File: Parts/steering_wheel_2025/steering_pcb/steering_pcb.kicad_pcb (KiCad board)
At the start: 2 copper layers, 102 x 102 mm, 189 parts, among them J0 Quick_connector, J1 Button 1 molex-µfit connector, J10 Button 1 molex-µfit connector, J11 Button 1 molex-µfit connector, J12 Button 1 molex-µfit connector, J13 PINHD_1x1_Male, J15 CAN pin header, J2 Button 1 molex-µfit connector, J3 Button 1 molex-µfit connector, J4 Button 1 molex-µfit connector, J5 Button 1 molex-µfit connector, J6 Button 1 molex-µfit connector, J7 Button 1 molex-µfit connector, J8 Button 1 molex-µfit connector, J9 Button 1 molex-µfit connector, Q1 BSS138BKS, Q10 2N7002DW, Q11 2N7002DW, Q12 2N7002DW, Q13 2N7002DW, Q14 2N7002DW, Q15 2N7002DW, Q16 2N7002DW, Q17 2N7002DW, Q18 2N7002DW, Q19 2N7002DW, Q2 2N7002DW, Q20 2N7002DW, Q21 2N7002DW, Q3 2N7002DW, Q4 BS170, Q5 2N7002DW, Q6 BSS138BKS, Q7 2N7002DW, Q8 2N7002DW, Q9 2N7002DW, SW1 Push_Button, U1 MCP2515-xSO, U2 TPS5430DDA, U3 TPS5430DDA, U5 ISM330DHCX, U6 TJA1051T-3, Y1 16MHz

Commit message: pcb progress backup
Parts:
- moved R84 434.1 mm to (132.4, 73.8), turned to 180 degrees
- moved J12 432.8 mm to (139.4, 82.7)
- moved R82 430.7 mm to (141.7, 75.1), turned to 0 degrees
- moved DZ12 427.7 mm to (138.3, 87.2), turned to 180 degrees
- moved R78 422.4 mm to (132.4, 68.5), turned to 0 degrees
- moved R81 419.3 mm to (144.8, 81.1), turned to 0 degrees
- moved D12 419.0 mm to (143.8, 87.2), turned to 0 degrees
- moved R76 416.9 mm to (151.9, 69.2), turned to 90 degrees
- moved J11 416.5 mm to (147.0, 68.0)
- moved Q21 415.3 mm to (145.1, 83.5), turned to 0 degrees
- moved Q19 413.6 mm to (150.0, 74.8)
- moved D11 413.4 mm to (146.8, 76.4)
- moved DZ11 413.3 mm to (146.8, 72.8)
- moved R75 412.6 mm to (149.4, 71.9), turned to 180 degrees
- moved R79 412.3 mm to (145.3, 79.2)
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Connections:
- net /LED and Buttons/Connector_5/button_2_0 renamed button10_0
- net /LED and Buttons/Connector_5/button_2_1 renamed button10_1
- net /LED and Buttons/Connector_5/button_2_2 renamed button10_2
- net /LED and Buttons/Connector_5/button_2_3 renamed button10_3
- net /LED and Buttons/Connector_6/button_1_0 renamed button11_0
- net /LED and Buttons/Connector_6/button_1_1 renamed button11_1
- net /LED and Buttons/Connector_6/button_1_2 renamed button11_2
- net /LED and Buttons/Connector_6/button_1_3 renamed button11_3
- net /LED and Buttons/Connector_6/button_2_0 renamed button12_0
- net /LED and Buttons/Connector_6/button_2_1 renamed button12_1
- net /LED and Buttons/Connector_6/button_2_2 renamed button12_2
- net /LED and Buttons/Connector_6/button_2_3 renamed button12_3
- A1 pad D10: unconnected-(A1-PadD10) -> button7_3
- A1 pad D11: unconnected-(A1-PadD11) -> button7_1
- A1 pad D12: unconnected-(A1-PadD12) -> button7_2
- A1 pad D13: unconnected-(A1-PadD13) -> button7_0
- A1 pad D14: unconnected-(A1-D14/TX3-PadD14) -> button9_3
- A1 pad D3: unconnected-(A1-D3_INT1-PadD3) -> button9_1
- A1 pad D4: unconnected-(A1-PadD4) -> button9_2
- A1 pad D5: unconnected-(A1-PadD5) -> button9_0
- A1 pad D6: unconnected-(A1-PadD6) -> button8_3
- A1 pad D7: unconnected-(A1-PadD7) -> button8_2
- A1 pad D8: unconnected-(A1-PadD8) -> button8_1
- A1 pad D9: unconnected-(A1-PadD9) -> button8_0
- D7 pad 4: /LED and Buttons/Connector_4/button_1_3 -> button7_3
- D7 pad 5: /LED and Buttons/Connector_4/button_1_2 -> button7_2
- D7 pad 6: /LED and Buttons/Connector_4/button_1_1 -> button7_1
- D8 pad 4: /LED and Buttons/Connector_4/button_2_3 -> button8_3
- D8 pad 5: /LED and Buttons/Connector_4/button_2_2 -> button8_2
- D8 pad 6: /LED and Buttons/Connector_4/button_2_1 -> button8_1
- D9 pad 4: /LED and Buttons/Connector_5/button_1_3 -> button9_3
- D9 pad 5: /LED and Buttons/Connector_5/button_1_2 -> button9_2
- D9 pad 6: /LED and Buttons/Connector_5/button_1_1 -> button9_1
- J7 pad 4: /LED and Buttons/Connector_4/button_1_0 -> button7_0
- J8 pad 4: /LED and Buttons/Connector_4/button_2_0 -> button8_0
- J9 pad 4: /LED and Buttons/Connector_5/button_1_0 -> button9_0
- Q13 pad 2: /LED and Buttons/Connector_4/button_1_2 -> button7_2
- Q13 pad 5: /LED and Buttons/Connector_4/button_1_1 -> button7_1
- Q14 pad 2: /LED and Buttons/Connector_4/button_1_3 -> button7_3
- Q14 pad 5: /LED and Buttons/Connector_4/button_2_1 -> button8_1
- Q15 pad 2: /LED and Buttons/Connector_4/button_2_2 -> button8_2
- Q15 pad 5: /LED and Buttons/Connector_4/button_2_3 -> button8_3
- Q16 pad 2: /LED and Buttons/Connector_5/button_1_2 -> button9_2
- Q16 pad 5: /LED and Buttons/Connector_5/button_1_1 -> button9_1
- Q17 pad 2: /LED and Buttons/Connector_5/button_1_3 -> button9_3
- R50 pad 1: /LED and Buttons/Connector_4/button_1_1 -> button7_1
- R52 pad 1: /LED and Buttons/Connector_4/button_1_0 -> button7_0
- R53 pad 2: /LED and Buttons/Connector_4/button_1_2 -> button7_2
- R55 pad 2: /LED and Buttons/Connector_4/button_1_3 -> button7_3
- R56 pad 2: /LED and Buttons/Connector_4/button_2_1 -> button8_1
- R58 pad 1: /LED and Buttons/Connector_4/button_2_0 -> button8_0
- R59 pad 2: /LED and Buttons/Connector_4/button_2_2 -> button8_2
- R61 pad 2: /LED and Buttons/Connector_4/button_2_3 -> button8_3
- R62 pad 1: /LED and Buttons/Connector_5/button_1_1 -> button9_1
- R64 pad 1: /LED and Buttons/Connector_5/button_1_0 -> button9_0
- R65 pad 2: /LED and Buttons/Connector_5/button_1_2 -> button9_2
- R67 pad 2: /LED and Buttons/Connector_5/button_1_3 -> button9_3
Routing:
- net button9_3: track 0.00 -> 24.5 mm
- net Net-(DZ10A-C1): track 9.13 -> 33.1 mm
- net Net-(DZ12A-C1): track 9.13 -> 33.1 mm
- net button9_2: track 0.00 -> 23.9 mm
- net button8_0: track 0.00 -> 23.5 mm
- net Net-(DZ11A-C1): track 22.6 -> 45.9 mm, vias 2 -> 4
- net Net-(DZ9A-C1): track 22.6 -> 45.9 mm, vias 2 -> 4
- net button10_0: track 11.5 -> 34.6 mm
- net button12_0: track 11.5 -> 34.6 mm
- net button12_1: track 7.15 -> 30.2 mm
- net button8_3: track 0.00 -> 20.7 mm, vias 0 -> 2
- net button8_1: track 0.00 -> 19.1 mm
- net Net-(DZ12B-C2): track 15.1 -> 32.9 mm, vias 2 -> 0
- net Net-(DZ10B-C2): track 15.1 -> 32.9 mm, vias 2 -> 0
- net button8_2: track 0.00 -> 17.8 mm
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- removed copper zone on B.Cu, net +7V
- removed copper zone on F.Cu, net LED_PWM

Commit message: PCB v1
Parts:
- moved Q19 52.1 mm to (190.7, 107.3), turned to 180 degrees
- moved R74 51.7 mm to (189.3, 110.2)
- moved D11 51.5 mm to (186.9, 108.7)
- moved J11 51.5 mm to (187.1, 100.3)
- moved Q20 51.5 mm to (190.5, 112.7)
- moved R75 51.5 mm to (189.5, 104.2)
- moved R81 51.5 mm to (184.9, 113.4)
- moved R84 51.5 mm to (172.4, 106.1)
- moved R78 51.5 mm to (172.4, 100.8)
- moved R82 51.5 mm to (181.8, 107.4)
- moved Q21 51.5 mm to (185.1, 115.8)
- moved R77 51.5 mm to (187.7, 111.7)
- moved R79 51.5 mm to (185.4, 111.5)
- moved DZ11 51.4 mm to (186.9, 104.9)
- moved R80 51.1 mm to (190.0, 115.8)
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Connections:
- A1 pad D1: unconnected-(A1-D1/TX0-PadD1) -> button10_0
- A1 pad D15: unconnected-(A1-D15/RX3-PadD15) -> button10_1
- A1 pad D16: unconnected-(A1-D16/TX2-PadD16) -> button10_2
- A1 pad D17: unconnected-(A1-D17/RX2-PadD17) -> button10_3
- A1 pad D18: unconnected-(A1-D18/TX1-PadD18) -> button11_0
- A1 pad D19: unconnected-(A1-D19/RX1-PadD19) -> button11_2
- A1 pad D20: unconnected-(A1-D20/SDA-PadD20) -> button11_1
- A1 pad D21: unconnected-(A1-D21/SCL-PadD21) -> button11_3
- A1 pad D48: button5_2 -> button5_3
- A1 pad D52: button5_3 -> button5_2
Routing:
- net Net-(DZ11A-C1): track 45.9 -> 17.9 mm, vias 4 -> 2
- net Net-(DZ9A-C1): track 45.9 -> 20.0 mm, vias 4 -> 2
- net button12_1: track 30.2 -> 11.2 mm
- net button12_0: track 34.6 -> 16.9 mm
- net Net-(DZ11B-C2): track 27.7 -> 10.6 mm, vias 4 -> 0
- net Net-(DZ9B-C2): track 27.7 -> 10.6 mm, vias 4 -> 0
- net button12_3: track 23.8 -> 7.11 mm, vias 4 -> 2
- net Net-(DZ12B-C2): track 32.9 -> 16.5 mm
- net Net-(DZ12A-C1): track 33.1 -> 17.2 mm
- net Net-(DZ10A-C1): track 33.1 -> 17.2 mm
- net Net-(DZ10B-C2): track 32.9 -> 17.2 mm
- net button8_3: track 20.7 -> 31.7 mm
- net Net-(DZ12C-C3): track 20.3 -> 10.1 mm
- net button9_3: track 24.5 -> 14.3 mm
- net Net-(DZ10C-C3): track 20.3 -> 10.6 mm
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
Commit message: KiCad after review 1
Spinat skal hjem og gro, Ost tager over og arbejder videre efter hans gode første review.
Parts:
- added J14: Conn_01x04_Pin, Connector_PinHeader_1.00mm:PinHeader_1x04_P1.00mm_Vertical, F.Cu at (258.0, 134.0)
- added J16: Conn_01x01_Pin, Connector_PinSocket_2.00mm:PinSocket_1x01_P2.00mm_Vertical, F.Cu at (261.2, 132.5)
- added R86: 10k, Resistor_SMD:R_0402_1005Metric_Pad0.72x0.64mm_HandSolder, F.Cu at (254.1, 129.7)
- added R87: 10k, Resistor_SMD:R_0402_1005Metric_Pad0.72x0.64mm_HandSolder, F.Cu at (254.1, 131.7)
- added R88: 10k, Resistor_SMD:R_0402_1005Metric_Pad0.72x0.64mm_HandSolder, F.Cu at (254.1, 133.7)
- added R89: 10k, Resistor_SMD:R_0402_1005Metric_Pad0.72x0.64mm_HandSolder, F.Cu at (254.1, 135.6)
- moved R30 21.4 mm to (268.5, 69.8), turned to 180 degrees
- moved R14 16.1 mm to (263.0, 40.5)
- moved R20 15.7 mm to (265.2, 68.1), turned to -90 degrees
- moved R36 8.30 mm to (267.5, 77.5), turned to 0 degrees
- moved R15 7.27 mm to (259.8, 48.8), turned to 0 degrees
- moved R25 5.66 mm to (250.0, 90.2), turned to -90 degrees
- moved JP1 2.16 mm to (211.7, 45.5), turned to 0 degrees
- moved R23 1.95 mm to (261.8, 50.0), turned to 90 degrees
- moved R24 1.80 mm to (250.5, 61.2)
- moved R28 1.65 mm to (264.2, 72.2)
- moved R19 1.54 mm to (249.3, 67.0)
- moved JP8 1.47 mm to (178.4, 129.8)
- moved R29 1.25 mm to (249.6, 87.2), turned to 90 degrees
- moved R8 1.23 mm to (209.0, 44.4), turned to 180 degrees
- moved J10 0.99 mm to (178.8, 86.8)
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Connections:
- A1 pad D22: unconnected-(A1-PadD22) -> button12_2
- A1 pad D23: LED_PWM_controller -> button12_0
- A1 pad D24: unconnected-(A1-PadD24) -> button12_1
- A1 pad D25: unconnected-(A1-PadD25) -> button12_3
- A1 pad D27: unconnected-(A1-PadD27) -> LED_PWM_controller
- A1 pad D30: unconnected-(A1-PadD30) -> Net-(J14-Pin_4)
- A1 pad D31: unconnected-(A1-PadD31) -> Net-(J14-Pin_3)
- A1 pad D32: unconnected-(A1-PadD32) -> Net-(J14-Pin_2)
- A1 pad D33: unconnected-(A1-PadD33) -> Net-(J14-Pin_1)
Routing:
- net LED_PWM: track 0.00 -> 269.8 mm, vias 0 -> 2
- net button12_3: track 7.11 -> 26.6 mm
- net button12_0: track 16.9 -> 28.0 mm
- net button2_0: track 59.9 -> 49.0 mm
- net button12_1: track 11.2 -> 21.5 mm
- net LED_PWM_controller: track 26.4 -> 36.3 mm
- net Net-(J4-Pin_6): track 5.20 -> 14.4 mm
- net button3_1: track 25.8 -> 17.1 mm
- net Net-(J3-Pin_6): track 7.81 -> 16.5 mm
- net button12_2: track 16.2 -> 24.2 mm
- net button3_2: track 24.9 -> 19.5 mm
- net Net-(J1-Pin_6): track 7.81 -> 12.6 mm
- net button1_0: track 48.1 -> 50.8 mm
- net +12V: track 92.2 -> 94.4 mm
- net Net-(J2-Pin_6): track 9.72 -> 7.98 mm
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
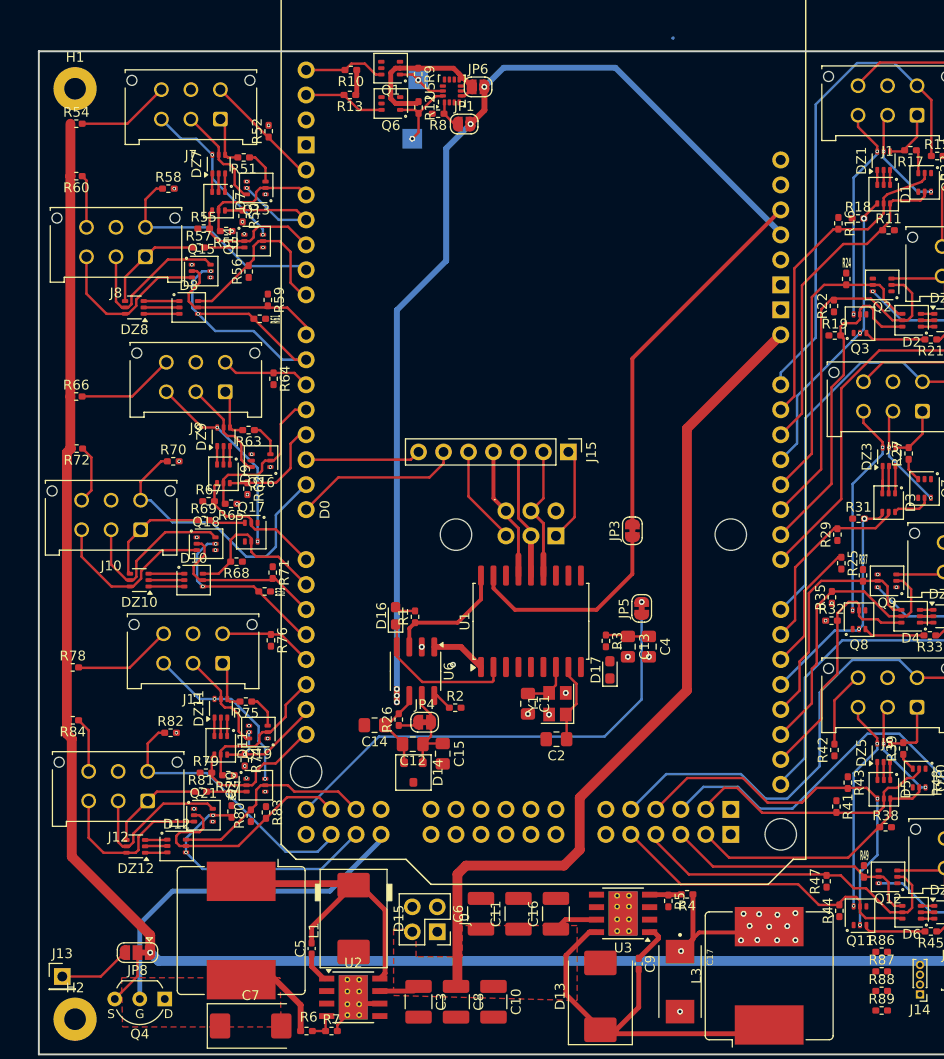
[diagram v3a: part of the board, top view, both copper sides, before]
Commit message: Kicad drawing update
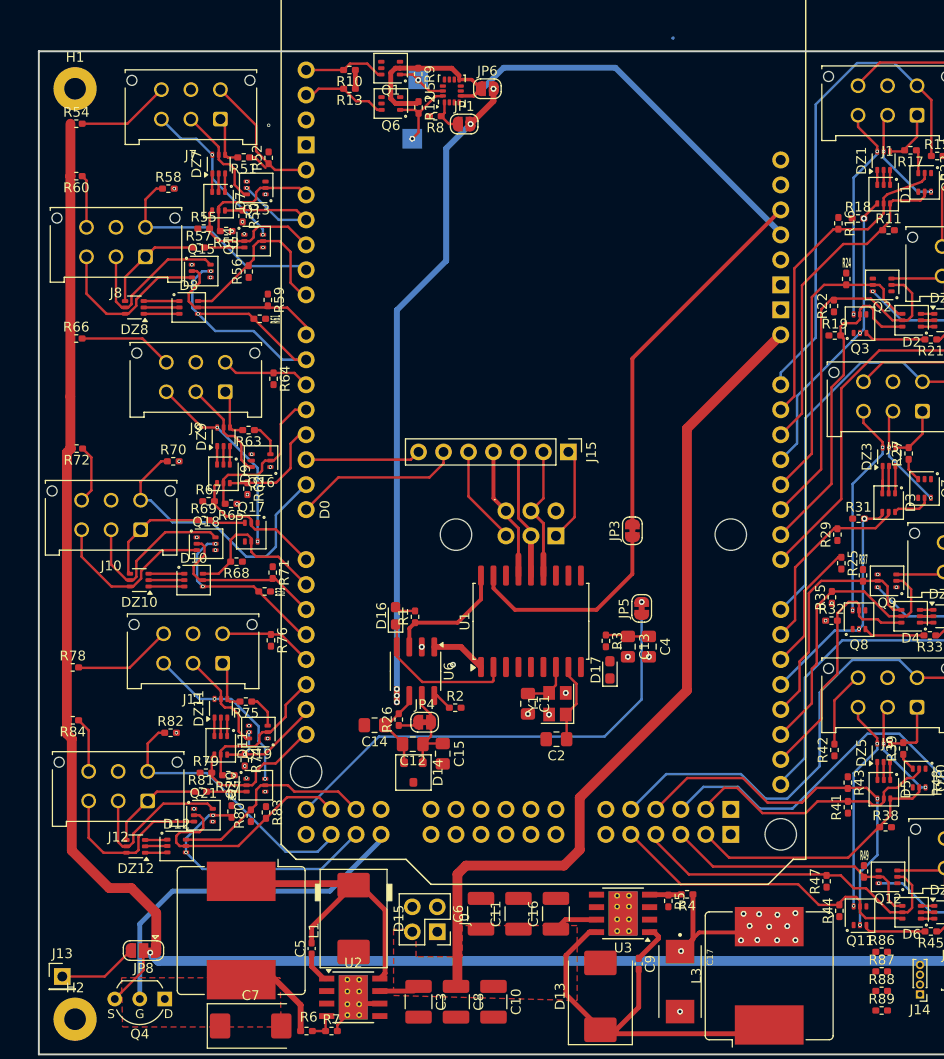
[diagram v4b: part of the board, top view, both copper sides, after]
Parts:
- moved R66 5.90 mm to (172.2, 67.3)
- moved R52 2.70 mm to (191.8, 48.9)
- moved R41 1.17 mm to (250.7, 115.0), turned to 90 degrees
- moved JP6 0.96 mm to (214.0, 41.9)
- moved JP8 0.64 mm to (179.0, 129.5)
- moved R13 0.64 mm to (200.0, 41.9)
- moved R8 0.38 mm to (208.7, 44.7)
- moved R10 0.14 mm to (200.0, 40.0)
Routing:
- net button7_0: track 12.1 -> 13.6 mm
- net Net-(Q13B-D2): track 3.46 -> 2.06 mm
- net LED_PWM: track 269.8 -> 271.2 mm
- net Net-(JP8-B): track 7.35 -> 8.04 mm
- net +5V: track 15.6 -> 14.9 mm
- net SDO: track 2.97 -> 3.56 mm
- net Net-(JP6-A): track 18.0 -> 18.6 mm
- net MCU_SDA: track 8.29 -> 8.82 mm

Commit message: PCB work update
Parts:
- moved J16 46.6 mm to (221.2, 108.5)
- moved R89 46.5 mm to (213.6, 112.8)
- moved J14 46.0 mm to (218.5, 110.5), turned to -90 degrees
- moved R88 43.6 mm to (215.9, 112.8), turned to 180 degrees
- moved R87 40.7 mm to (218.1, 112.8)
- moved R86 37.8 mm to (220.3, 112.8), turned to 180 degrees
- moved R42 20.7 mm to (267.5, 99.2), turned to 180 degrees
- moved R20 18.3 mm to (261.8, 50.1)
- moved R23 17.7 mm to (265.9, 67.2), turned to 180 degrees
- moved R84 10.1 mm to (181.9, 106.8)
- moved R70 10.0 mm to (172.2, 78.5)
- moved R82 9.89 mm to (172.0, 106.0)
- moved R72 9.88 mm to (182.1, 79.2)
- moved R58 9.32 mm to (172.3, 50.8)
- moved R60 9.22 mm to (181.4, 51.5)
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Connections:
- A1 pad D30: Net-(J14-Pin_4) -> unconnected-(A1-PadD30)
- A1 pad D31: Net-(J14-Pin_3) -> unconnected-(A1-PadD31)
- A1 pad D32: Net-(J14-Pin_2) -> unconnected-(A1-PadD32)
- A1 pad D33: Net-(J14-Pin_1) -> unconnected-(A1-PadD33)
- A1 pad D34: unconnected-(A1-PadD34) -> Net-(J14-Pin_4)
- A1 pad D36: unconnected-(A1-PadD36) -> Net-(J14-Pin_3)
- A1 pad D38: unconnected-(A1-PadD38) -> Net-(J14-Pin_2)
- A1 pad D40: unconnected-(A1-PadD40) -> Net-(J14-Pin_1)
- J0 pad 2: CAN_L -> CAN_H
- J0 pad 4: CAN_H -> CAN_L
- R20 pad 1: button2_0 -> LED_PWM
- R20 pad 2: GND -> Net-(J2-Pin_6)
- R23 pad 1: Net-(J2-Pin_6) -> GND
- R23 pad 2: LED_PWM -> button2_0
- R34 pad 1: button4_0 -> LED_PWM
- R34 pad 2: GND -> Net-(J4-Pin_6)
- R36 pad 1: Net-(J4-Pin_6) -> GND
- R36 pad 2: LED_PWM -> button4_0
- R46 pad 1: button6_0 -> LED_PWM
- R46 pad 2: GND -> Net-(J6-Pin_6)
- R48 pad 1: Net-(J6-Pin_6) -> GND
- R48 pad 2: LED_PWM -> button6_0
- R58 pad 1: button8_0 -> LED_PWM
- R58 pad 2: GND -> Net-(J8-Pin_6)
- R60 pad 1: Net-(J8-Pin_6) -> GND
- R60 pad 2: LED_PWM -> button8_0
- R70 pad 1: button10_0 -> LED_PWM
- R70 pad 2: GND -> Net-(J10-Pin_6)
- R72 pad 1: Net-(J10-Pin_6) -> GND
- R72 pad 2: LED_PWM -> button10_0
- R82 pad 1: button12_0 -> LED_PWM
- R82 pad 2: GND -> Net-(J12-Pin_6)
- R84 pad 1: Net-(J12-Pin_6) -> GND
- R84 pad 2: LED_PWM -> button12_0
- R86 pad 2: Net-(J14-Pin_4) -> Net-(J14-Pin_1)
- R87 pad 2: Net-(J14-Pin_3) -> Net-(J14-Pin_2)
- R88 pad 2: Net-(J14-Pin_2) -> Net-(J14-Pin_3)
- R89 pad 2: Net-(J14-Pin_1) -> Net-(J14-Pin_4)
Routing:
- net +7V: track 17.1 -> 186.5 mm
- net +5V_MCU: track 48.7 -> 89.3 mm
- net Net-(JP5-A): track 17.2 -> 39.2 mm
- net CAN_H: track 9.60 -> 25.4 mm
- net CAN_L: track 8.82 -> 23.8 mm
- net Net-(U1-TXCAN): track 5.60 -> 19.4 mm
- net +5V: track 14.9 -> 3.34 mm
- net GND: track 3.72 -> 12.4 mm, vias 38 -> 44
- net Net-(J5-Pin_6): track 7.81 -> 16.3 mm
- net LED_PWM: track 271.2 -> 278.6 mm
- net Net-(J6-Pin_6): track 5.20 -> 11.3 mm
- net Net-(J14-Pin_1): track 0.00 -> 5.72 mm
- net Net-(J14-Pin_4): track 0.00 -> 5.58 mm
- net Net-(J14-Pin_3): track 0.00 -> 5.46 mm
- net Net-(J14-Pin_2): track 0.00 -> 5.29 mm
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- added copper zone on B.Cu, net +7V

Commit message: Update steering_pcb.kicad_pcb
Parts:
- moved R23 19.8 mm to (250.6, 79.8)
- moved R32 12.7 mm to (246.3, 108.4), turned to 90 degrees
- moved R25 4.41 mm to (253.9, 88.2)
- moved R61 3.15 mm to (192.4, 68.0), turned to 90 degrees
- moved R29 2.63 mm to (251.1, 85.0), turned to -90 degrees
- moved R31 1.23 mm to (252.7, 84.8), turned to -90 degrees
- moved R24 1.10 mm to (249.4, 61.2)
- moved R37 1.05 mm to (251.2, 91.3)
- moved R46 0.95 mm to (267.6, 112.2)
- moved R19 0.40 mm to (249.3, 67.4), turned to 180 degrees
- moved R22 0.25 mm to (249.0, 64.0), turned to 0 degrees
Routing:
- net +7V: track 186.5 -> 395.4 mm
- net GND: track 12.4 -> 41.9 mm, vias 44 -> 68
- net ~{RESET}: track 38.2 -> 60.2 mm, vias 0 -> 1
- net button3_1: track 17.1 -> 26.0 mm
- net button5_0: track 47.6 -> 44.9 mm
- net Net-(DZ1B-C2): track 10.8 -> 12.9 mm
- net button3_0: track 41.6 -> 40.0 mm
- net LED_PWM_controller: track 36.3 -> 34.8 mm, vias 0 -> 1
- net Net-(J6-Pin_6): track 11.3 -> 10.2 mm
- net button2_1: track 33.1 -> 34.1 mm
- net button3_2: track 19.5 -> 20.4 mm
- net button6_0: track 45.0 -> 45.7 mm
- net button2_2: track 37.6 -> 36.9 mm
- net LED_PWM: track 278.6 -> 278.0 mm
- net Net-(J12-Pin_6): vias 1 -> 0
